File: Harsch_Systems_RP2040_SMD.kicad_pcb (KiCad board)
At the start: 2 copper layers, 163 parts, among them J1 Jack-DC, J2 Conn_01x02_Male, J3 Conn_01x08_Female, J4 Conn_01x08_Female, J5 Conn_01x04_Female, J6 Conn_01x06_Female, J7 USB_A, J8 DEBUG, Q1 BSS123, Q2 BSS123, Q3 BSS123, Q4 BSS123, Q5 BCP56, Q6 BCP56, Q7 BCP56, Q8 BCP56, SW1 SW_MEC_5E, U1 XC6210B332MR, U10 TLV9304IDR, U2 TPS62933, U3 RP2040, U4 W25Q32JVSSIQ_TR, U5 TLV9004xRUCR, U6 ELQ3H7, U7 TLV9004xRUCR, U8 ELQ3H7, U9 ELQ3H7, Y1 12MHz

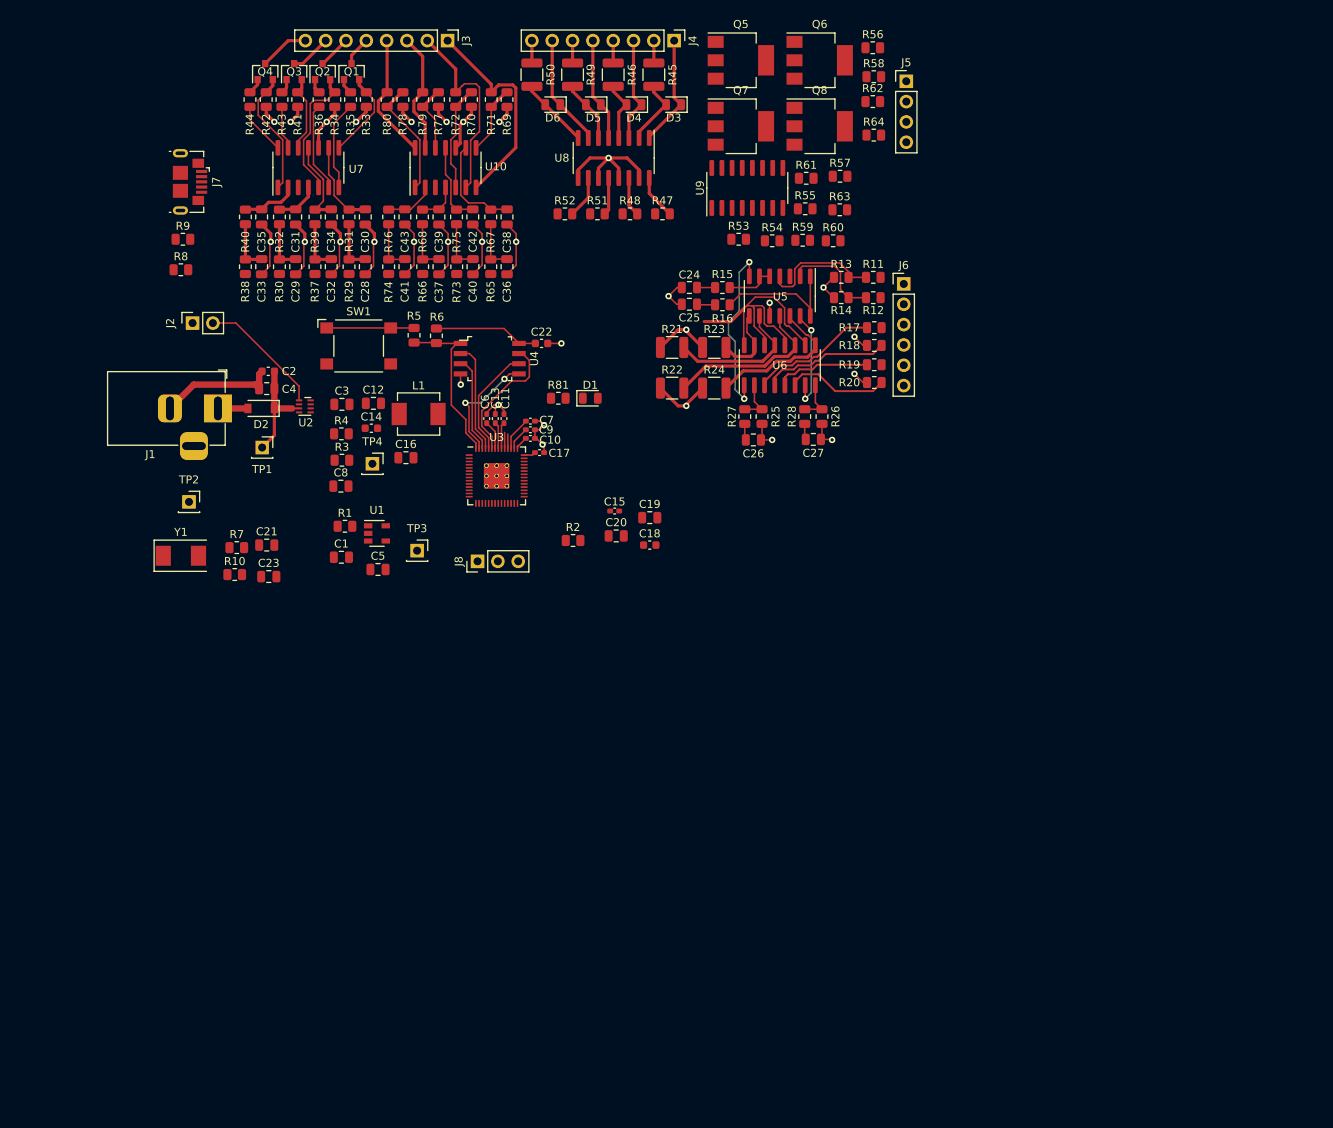
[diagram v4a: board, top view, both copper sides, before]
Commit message: Power circuitry routing and board outline
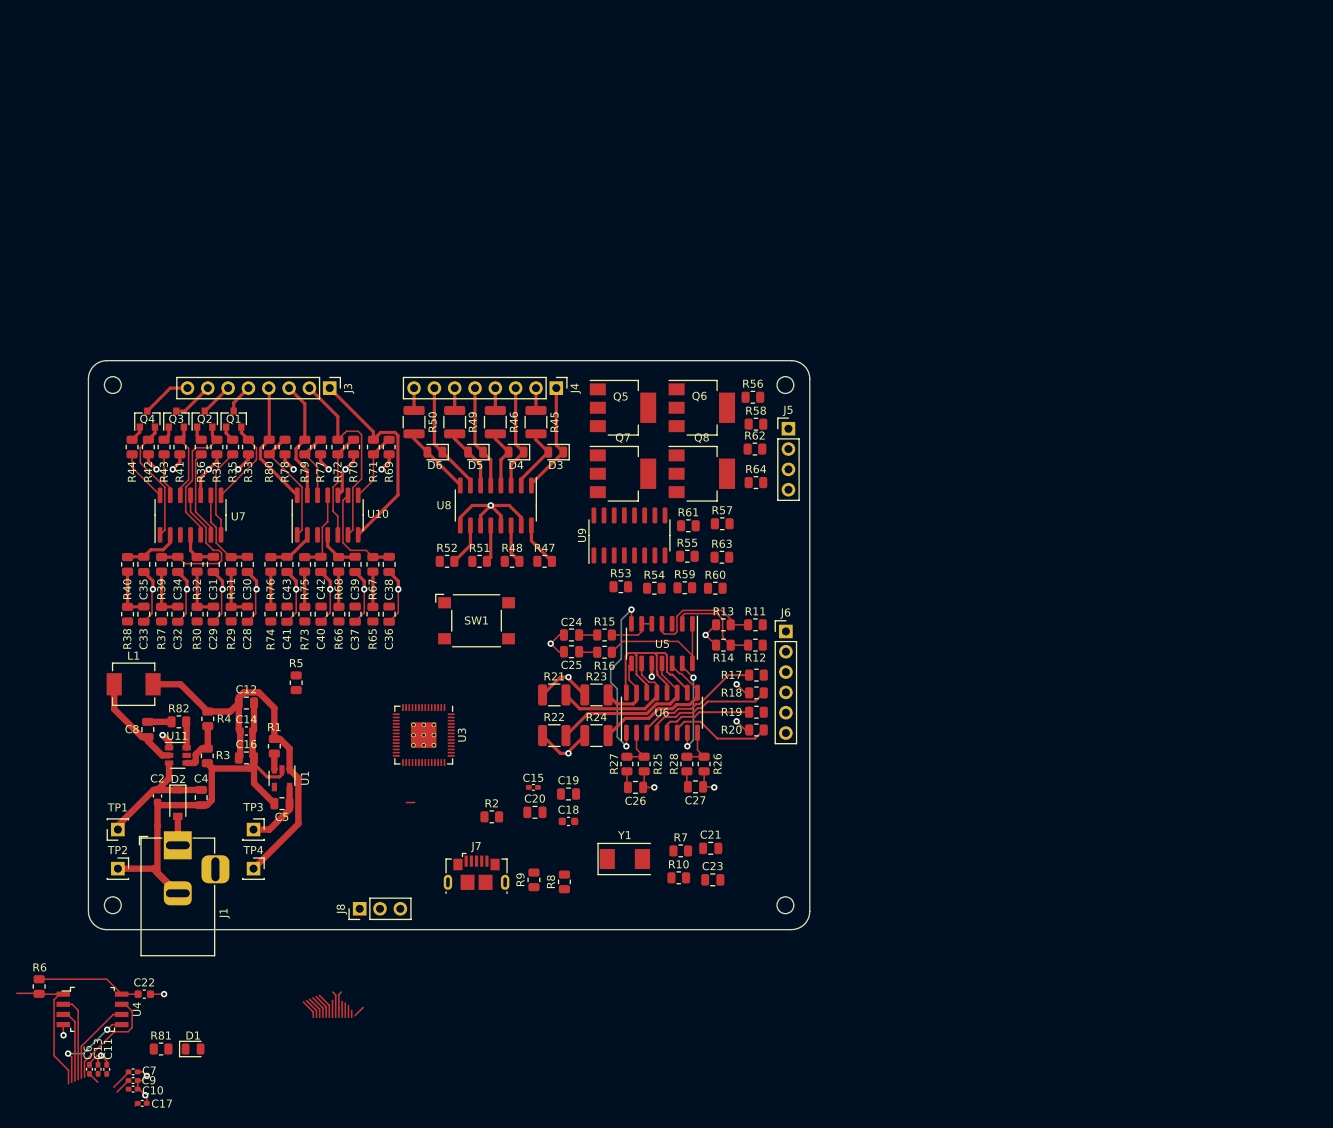
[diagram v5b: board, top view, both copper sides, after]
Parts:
- removed C1: 1μ, Capacitor_SMD:C_0805_2012Metric
- removed C3: 33n, Capacitor_SMD:C_0805_2012Metric
- removed J2: Conn_01x02_Male, Connector_PinSocket_2.54mm:PinSocket_1x02_P2.54mm_Vertical
- removed U2: TPS62933, Package_DFN_QFN:Texas_VSON-HR-8_1.5x2mm_P0.5mm
- added R82: 10, Resistor_SMD:R_0805_2012Metric, F.Cu at (101.7, 99.3)
- added REF**: MountingHole_2.1mm, MountingHole:MountingHole_2.1mm, F.Cu at (93.5, 57.1)
- added REF**: MountingHole_2.1mm, MountingHole:MountingHole_2.1mm, F.Cu at (177.5, 57.1)
- added REF**: MountingHole_2.1mm, MountingHole:MountingHole_2.1mm, F.Cu at (93.5, 122.2)
- added REF**: MountingHole_2.1mm, MountingHole:MountingHole_2.1mm, F.Cu at (177.5, 122.2)
- added U11: TPS56339DDC, Package_TO_SOT_SMD:SOT-23-6, F.Cu at (101.6, 103.4)
- C8: value 33n -> .1μ
- L1: value 6.8μ -> 5.6μ
- R4: value 53.6k -> 52.3k
- moved C11 95.3 mm to (92.7, 142.7)
- moved C10 95.3 mm to (96.0, 145.2)
- moved C7 95.3 mm to (96.0, 143.0)
- moved C9 95.3 mm to (96.0, 144.1)
- moved R6 95.3 mm to (84.3, 132.3)
- moved C13 95.3 mm to (91.6, 142.7)
- moved C17 95.3 mm to (97.2, 146.9)
- moved C22 95.3 mm to (97.4, 133.3)
- moved C6 95.3 mm to (90.6, 142.7)
- moved D1 95.3 mm to (103.5, 140.1)
- moved R81 95.3 mm to (99.5, 140.1)
- moved U4 95.3 mm to (90.9, 135.2)
- moved J7 93.5 mm to (138.9, 118.1), turned to 0 degrees
- moved R9 91.3 mm to (146.1, 119.0), turned to 90 degrees
- moved R8 90.3 mm to (149.9, 119.3), turned to 90 degrees
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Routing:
- net +5V: track 0.00 -> 49.9 mm
- net GND: track 165.1 -> 210.4 mm, vias 31 -> 32
- net Net-(J2-Pad2): track 15.8 -> 0.00 mm
- net Net-(C8-Pad2): track 0.00 -> 12.7 mm
- net Net-(R5-Pad2): track 10.9 -> 0.00 mm
- net 3.3V: track 37.0 -> 27.3 mm
- net +3V3: track 25.9 -> 34.0 mm
- net Net-(C34-Pad1): track 11.0 -> 18.3 mm
- net Net-(R3-Pad2): track 0.00 -> 6.69 mm
- net Net-(R82-Pad2): track 0.00 -> 3.27 mm
- net +24V: track 13.2 -> 16.3 mm
- net Net-(C8-Pad1): track 0.00 -> 2.96 mm
- net Net-(C40-Pad1): track 6.46 -> 4.46 mm
- net Net-(C37-Pad1): track 6.46 -> 4.46 mm
- net Net-(C41-Pad1): track 6.45 -> 4.45 mm
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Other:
- board outline added: 90.2 x 71.1 mm

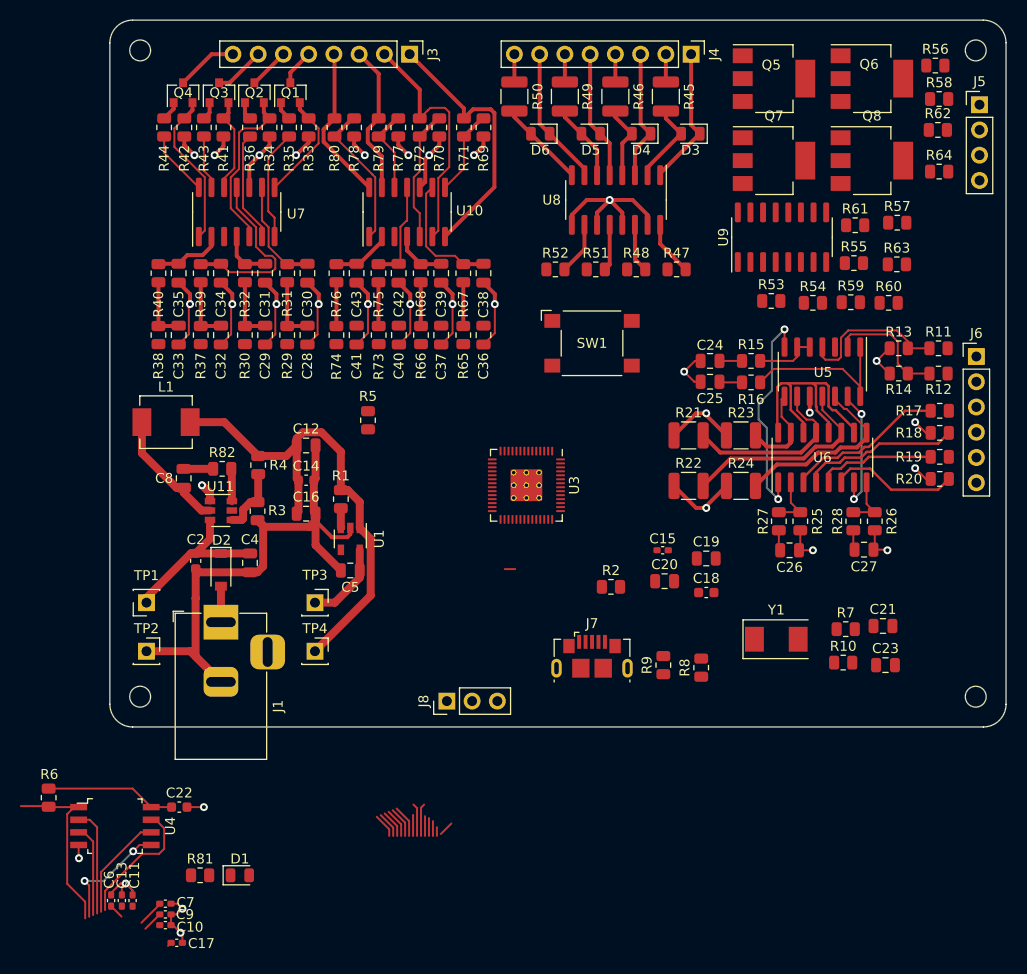
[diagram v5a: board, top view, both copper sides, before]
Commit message: Everything but the 24V output is routed
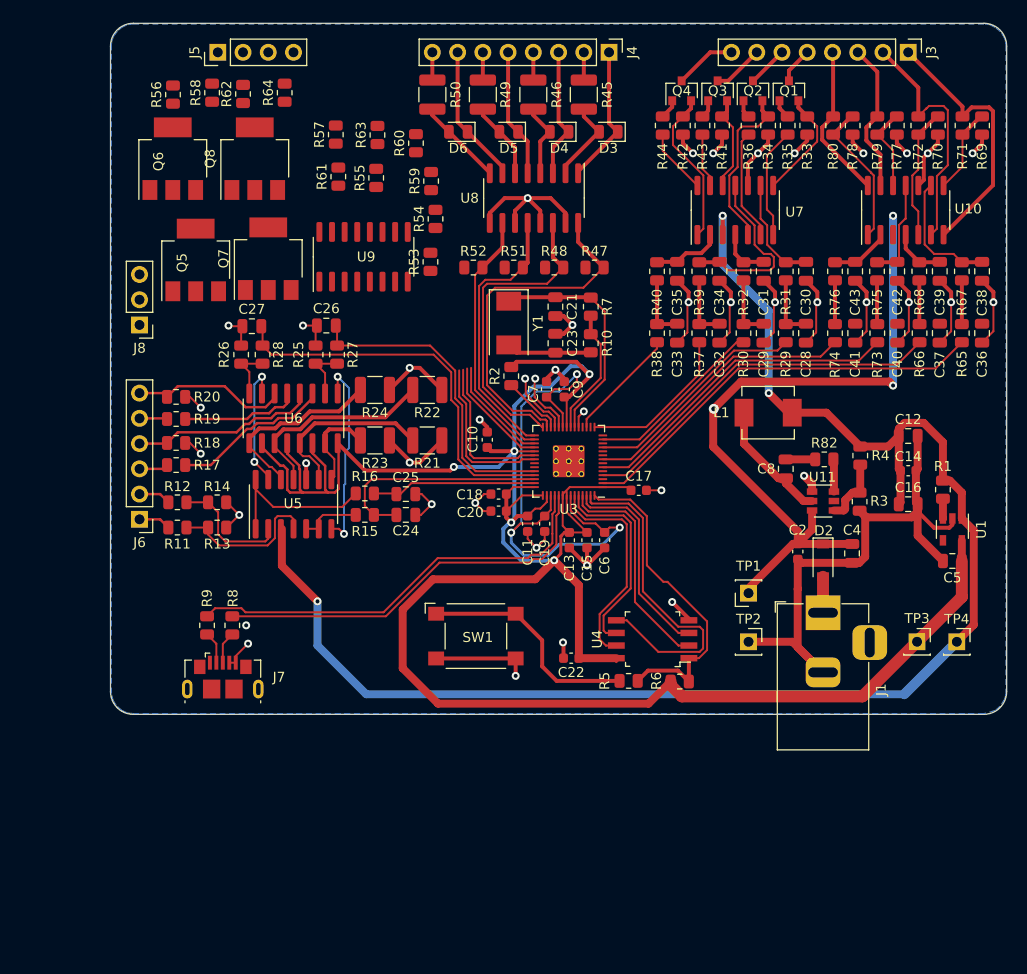
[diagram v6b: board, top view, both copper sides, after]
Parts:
- removed D1: LED, LED_SMD:LED_0805_2012Metric
- removed R81: 470, Resistor_SMD:R_0805_2012Metric
- removed REF** (x4): MountingHole_2.1mm, MountingHole:MountingHole_2.1mm
- C10, C11, C13, C15, C17, C6, C7, C9: footprint Capacitor_SMD:C_0402_1005Metric_Pad0.74x0.62mm_HandSolder -> Capacitor_SMD:C_0603_1608Metric
- C19, C20: footprint Capacitor_SMD:C_0805_2012Metric -> Capacitor_SMD:C_0603_1608Metric
- moved J6 85.8 mm to (93.4, 104.3), turned to 180 degrees
- moved R11 78.7 mm to (97.2, 105.2), turned to 180 degrees
- moved R12 77.7 mm to (97.2, 102.6), turned to 180 degrees
- moved R20 77.3 mm to (97.1, 92.0), turned to 180 degrees
- moved R17 77.0 mm to (97.1, 98.9), turned to 180 degrees
- moved R19 76.9 mm to (97.1, 94.2), turned to 180 degrees
- moved R18 76.8 mm to (97.1, 96.6), turned to 180 degrees
- moved J5 76.8 mm to (101.3, 57.3), turned to 90 degrees
- moved R56 76.8 mm to (96.8, 61.6), turned to 90 degrees
- moved R58 73.2 mm to (100.7, 61.4), turned to 90 degrees
- moved R13 70.9 mm to (101.2, 105.2), turned to 180 degrees
- moved Q6 70.8 mm to (96.8, 68.0), turned to 90 degrees
- moved R62 70.0 mm to (103.8, 61.5), turned to 90 degrees
- moved R14 69.8 mm to (101.2, 102.6), turned to 180 degrees
- moved C9 66.3 mm to (136.1, 91.2), turned to 90 degrees
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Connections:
- net /USB_DM renamed /USB_D-
- net /USB_DP renamed /USB_D+
- C24 pad 1: /ADC0 -> /ADC2
- C25 pad 1: /ADC1 -> /ADC3
- C26 pad 1: /ADC2 -> /ADC0
- C27 pad 1: /ADC3 -> /ADC1
- Q5 pad 2: 24V -> +24V
- Q5 pad 4: 24V -> +24V
- Q6 pad 2: 24V -> +24V
- Q6 pad 4: 24V -> +24V
- Q7 pad 2: 24V -> +24V
- Q7 pad 4: 24V -> +24V
- Q8 pad 2: 24V -> +24V
- Q8 pad 4: 24V -> +24V
- R15 pad 1: /ADC0 -> /ADC2
- R16 pad 1: /ADC1 -> /ADC3
- R27 pad 1: /ADC2 -> /ADC0
- R28 pad 1: /ADC3 -> /ADC1
- R47 pad 2: /GPIO1 -> /GPIO16
- R48 pad 2: /GPIO3 -> /GPIO17
- R51 pad 2: /GPIO5 -> /GPIO18
- R52 pad 2: /GPIO7 -> /GPIO19
- U3 pad 12: /GPIO9 -> Net-(U3-Pad12)
- U3 pad 14: /GPIO11 -> Net-(U3-Pad14)
- U3 pad 16: /GPIO13 -> Net-(U3-Pad16)
- U3 pad 18: /GPIO15 -> Net-(U3-Pad18)
- U3 pad 27: Net-(U3-Pad27) -> /GPIO16
- U3 pad 28: Net-(U3-Pad28) -> /GPIO17
- U3 pad 29: Net-(U3-Pad29) -> /GPIO18
- U3 pad 3: /GPIO1 -> Net-(U3-Pad3)
- U3 pad 30: Net-(U3-Pad30) -> /GPIO19
- U3 pad 31: Net-(U3-Pad31) -> /GPIO20
- U3 pad 32: Net-(U3-Pad32) -> /GPIO21
- U3 pad 34: Net-(U3-Pad34) -> /GPIO22
- U3 pad 35: Net-(U3-Pad35) -> /GPIO23
- U3 pad 37: /GPIO25 -> Net-(U3-Pad37)
- U3 pad 5: /GPIO3 -> Net-(U3-Pad5)
- U3 pad 7: /GPIO5 -> Net-(U3-Pad7)
- U3 pad 9: /GPIO7 -> Net-(U3-Pad9)
- U6 pad 10: 3.3V -> +3V3
- U6 pad 12: 3.3V -> +3V3
- U6 pad 14: 3.3V -> +3V3
- U6 pad 16: 3.3V -> +3V3
- U8 pad 10: /GPIO7 -> /GPIO19
- U8 pad 12: /GPIO5 -> /GPIO18
- U8 pad 14: /GPIO3 -> /GPIO17
- U8 pad 16: /GPIO1 -> /GPIO16
- U9 pad 1: /GPIO9 -> /GPIO23
- U9 pad 10: 24V -> +24V
- U9 pad 11: Net-(R61-Pad1) -> Net-(R57-Pad1)
- U9 pad 12: 24V -> +24V
- U9 pad 13: Net-(R57-Pad1) -> Net-(R61-Pad1)
- U9 pad 14: 24V -> +24V
- U9 pad 15: Net-(R55-Pad1) -> Net-(R63-Pad1)
- U9 pad 16: 24V -> +24V
- U9 pad 2: Net-(R53-Pad2) -> Net-(R60-Pad2)
- U9 pad 3: /GPIO11 -> /GPIO22
- U9 pad 4: Net-(R54-Pad2) -> Net-(R59-Pad2)
- U9 pad 5: /GPIO13 -> /GPIO21
- U9 pad 6: Net-(R59-Pad2) -> Net-(R54-Pad2)
- U9 pad 7: /GPIO15 -> /GPIO20
- U9 pad 8: Net-(R60-Pad2) -> Net-(R53-Pad2)
- U9 pad 9: Net-(R63-Pad1) -> Net-(R55-Pad1)
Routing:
- net +3V3: track 34.0 -> 242.4 mm, vias 0 -> 5
- net +5V: track 49.9 -> 154.9 mm, vias 0 -> 3
- net +24V: track 16.3 -> 69.9 mm, vias 0 -> 3
- net +1V1: track 7.76 -> 55.9 mm, vias 0 -> 3
- net /PWM0: track 0.00 -> 42.0 mm
- net /USB_D-: track 1.80 -> 43.0 mm
- net /USB_D+: track 1.99 -> 40.7 mm
- net /PWM1: track 0.00 -> 37.4 mm
- net /ADC1: track 2.29 -> 39.5 mm
- net /GPIO16: track 0.00 -> 35.6 mm
- net /PWM2: track 0.00 -> 32.8 mm
- net /GPIO17: track 0.00 -> 31.5 mm
- net GND: track 210.4 -> 240.2 mm, vias 32 -> 40
- net /ADC0: track 2.27 -> 31.9 mm
- net /PWM3: track 0.00 -> 28.2 mm
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- added copper zone on B.Cu, net GND
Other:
- board size 90.2 x 71.1 mm -> 90.2 x 69.5 mm

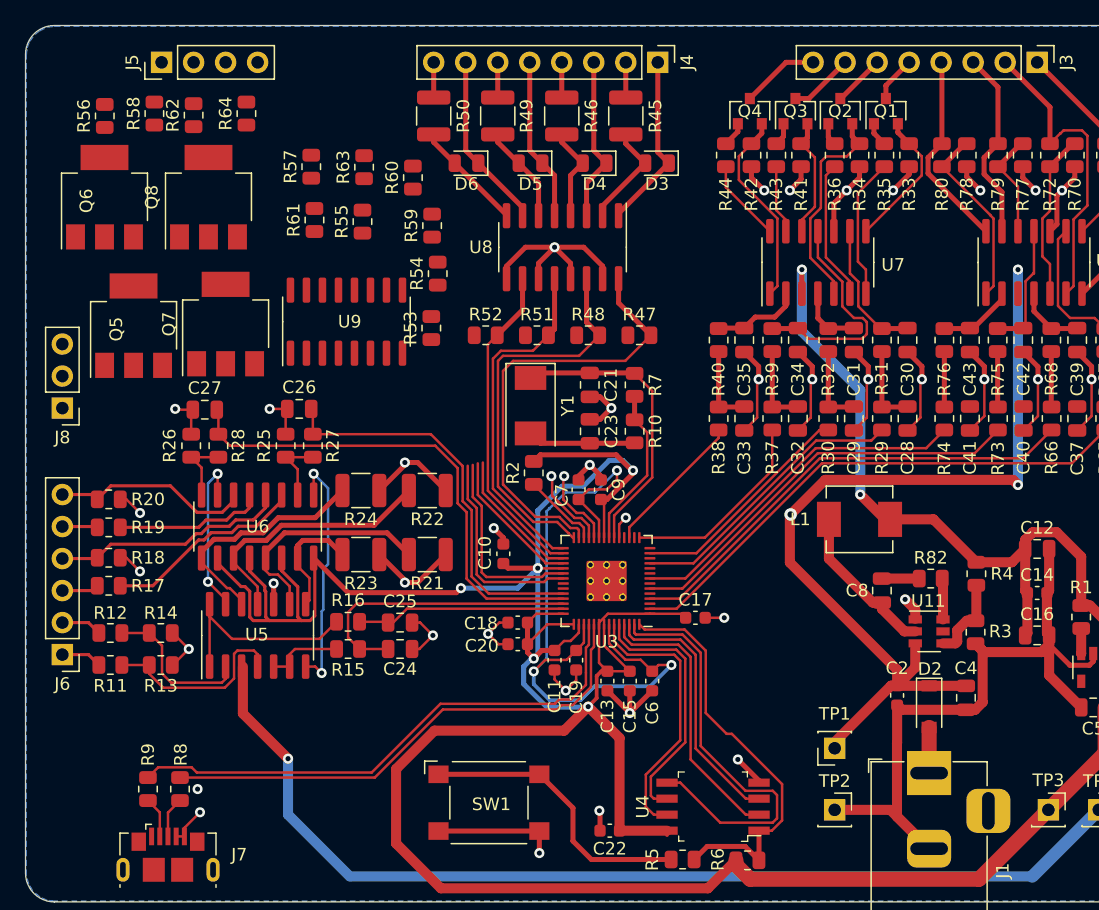
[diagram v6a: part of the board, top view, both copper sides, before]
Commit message: Finished routing, but realized an optocoupler on 24V outputs isn't rated high enough
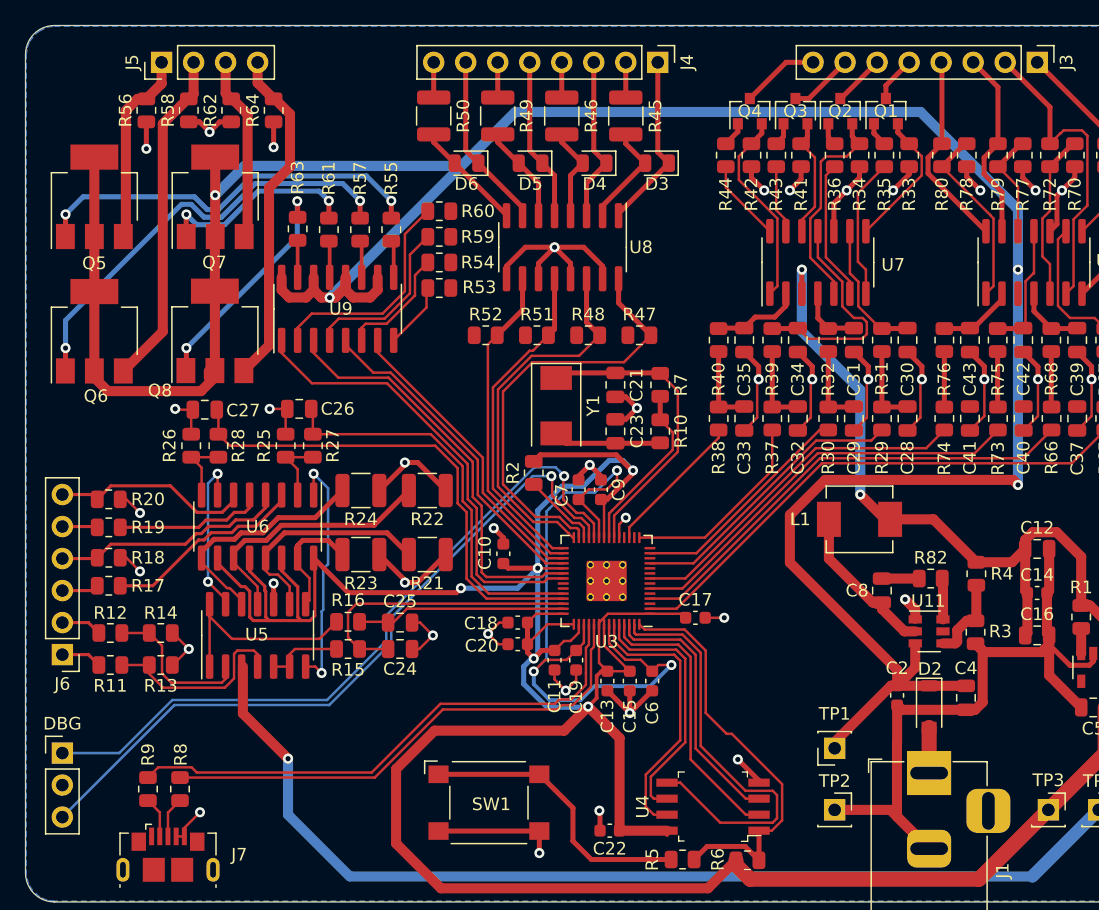
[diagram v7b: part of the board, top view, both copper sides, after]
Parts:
- moved DBG 27.4 mm to (93.4, 112.1), turned to 0 degrees
- moved Q5 10.7 mm to (95.9, 68.0)
- moved Q6 10.7 mm to (95.9, 78.7)
- moved Q8 10.6 mm to (105.5, 78.6)
- moved Q7 10.1 mm to (105.5, 68.0)
- moved R63 7.19 mm to (112.1, 70.5)
- moved R57 6.32 mm to (117.0, 70.6)
- moved R60 3.39 mm to (123.3, 69.2), turned to 180 degrees
- moved R56 3.33 mm to (100.1, 61.2)
- moved R53 3.24 mm to (123.3, 75.2), turned to 180 degrees
- moved R62 3.01 mm to (106.8, 61.2)
- moved R58 2.74 mm to (103.4, 61.2)
- moved R55 2.37 mm to (119.5, 70.6)
- moved R64 2.17 mm to (110.2, 61.2)
- moved C21 2.03 mm to (137.3, 82.9)
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- renumbered J8 to DBG
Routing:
- net +24V: track 69.9 -> 219.0 mm, vias 3 -> 4
- net /SWDIO: track 6.43 -> 57.7 mm
- net /SWCLK: track 6.23 -> 57.0 mm
- net Net-(Q6-Pad1): track 0.00 -> 34.7 mm, vias 0 -> 2
- net Net-(Q5-Pad1): track 0.00 -> 31.9 mm, vias 0 -> 2
- net /Digital Output/OUT3: track 0.00 -> 27.1 mm
- net /Digital Output/OUT1: track 0.00 -> 26.8 mm
- net /GPIO23: track 16.2 -> 35.7 mm
- net Net-(Q8-Pad1): track 0.00 -> 18.4 mm, vias 0 -> 2
- net Net-(R60-Pad2): track 0.00 -> 17.8 mm
- net /GPIO22: track 15.6 -> 33.0 mm
- net Net-(Q7-Pad1): track 0.00 -> 16.2 mm, vias 0 -> 2
- net /Digital Output/OUT0: track 0.00 -> 15.5 mm
- net /GPIO21: track 11.6 -> 26.5 mm
- net /Digital Output/OUT2: track 0.00 -> 14.7 mm
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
